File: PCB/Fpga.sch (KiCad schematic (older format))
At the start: 0 parts

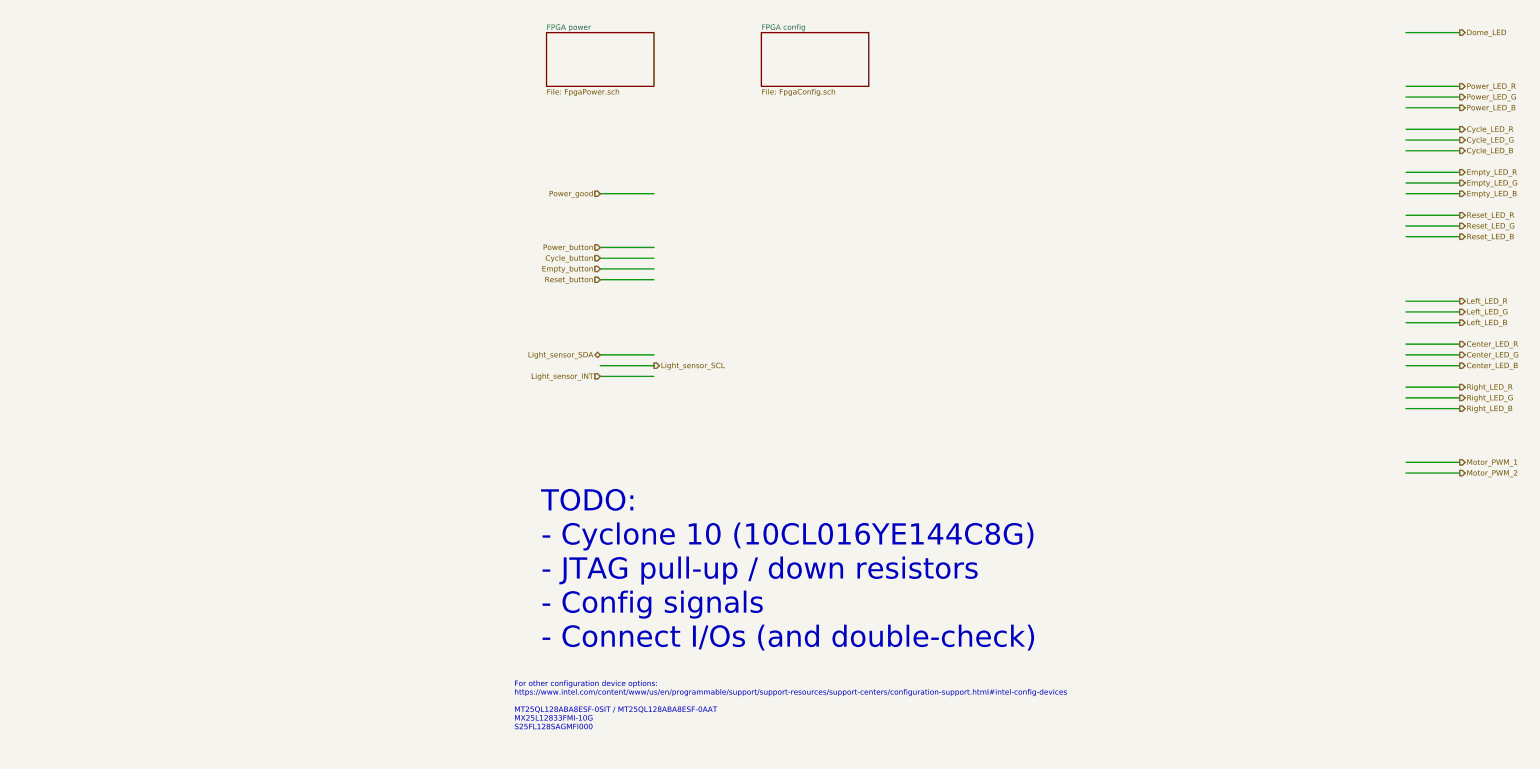
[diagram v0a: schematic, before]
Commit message: Connect the FPGA configuration signals
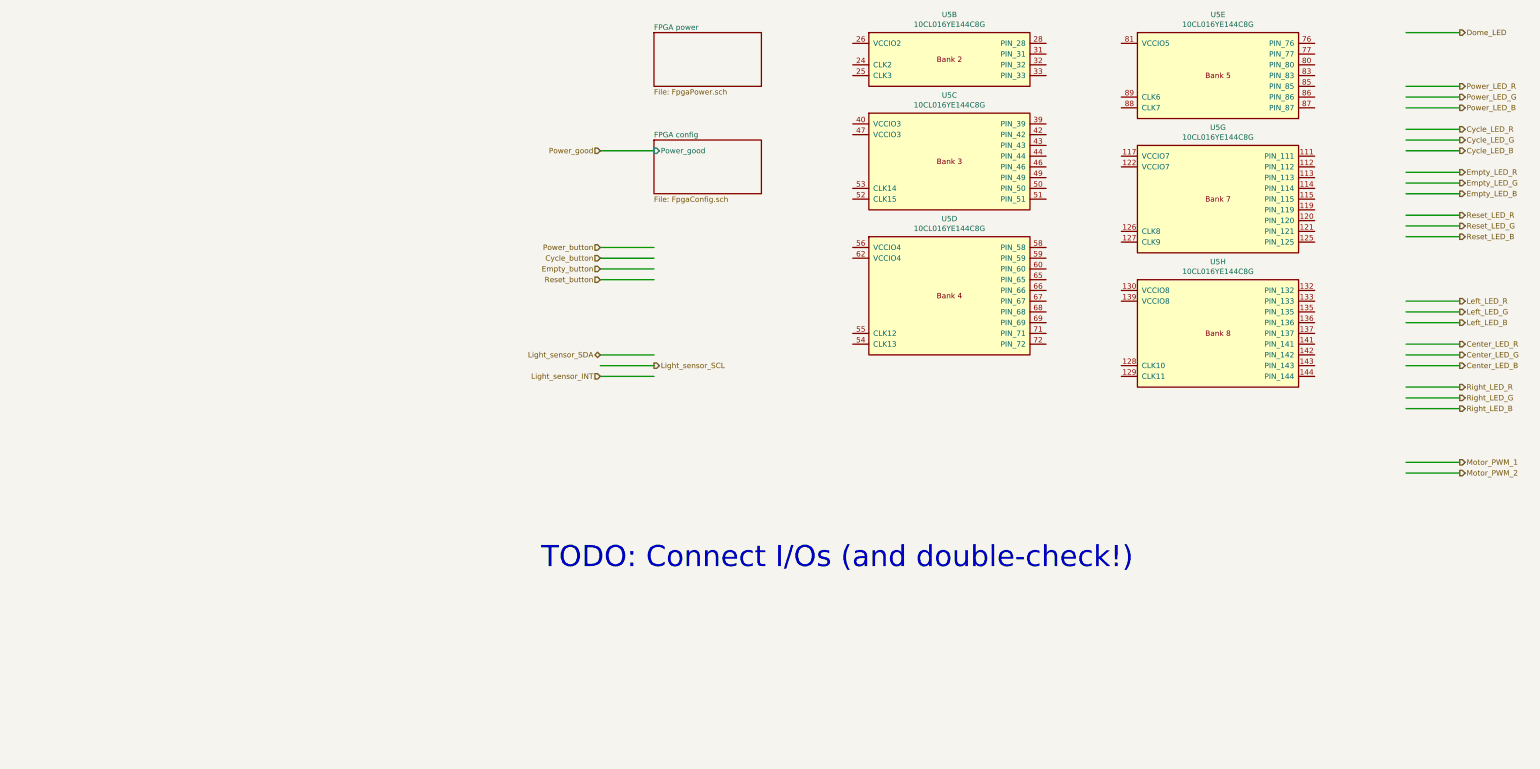
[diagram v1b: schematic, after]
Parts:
- added U5: 10CL016YE144C8G, LitterRobot:Intel_EQFP-144-1EP_20x20mm_P0.5mm_EP6.7x6.7mm, symbol LitterRobot:10CLxxxYE144
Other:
- note added: "TODO: Connect I/Os (and double-check!)"
- note removed: "For other configuration device options:\nhttps://www.intel.com/content/www/us/en/programmable/support/support-resources/support-centers/configuration-support.html#intel-config-devices\n\nMT25QL128ABA8ESF-0SIT / MT25QL128ABA8ESF-0AAT\nMX25L12833FMI-10G\nS25FL128SAGMFI000"
- note removed: "TODO:\n- Cyclone 10 (10CL016YE144C8G)\n- JTAG pull-up / down resistors\n- Config signals\n- Connect I/Os (and double-check)"
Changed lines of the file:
@@
 Wire Wire Line
 	1500 3300 2000 3300
-Text HLabel 1500 2500 0    50   Input ~ 0
+Text HLabel 1500 2100 0    50   Input ~ 0
 Power_good
 Wire Wire Line
-	1500 2500 2000 2500
+	1500 2100 2000 2100
 Wire Wire Line
 	9500 1700 9000 1700
@@
 Text HLabel 9500 5000 2    50   Output ~ 0
 Motor_PWM_1
-Text Notes 950  6750 0    197  ~ 0
-TODO:\n- Cyclone 10 (10CL016YE144C8G)\n- JTAG pull-up / down resistors\n- Config signals\n- Connect I/Os (and double-check)
+Text Notes 950  6000 0    197  ~ 0
+TODO: Connect I/Os (and double-check!)
 Wire Wire Line
 	9000 1000 9500 1000
@@
 Wire Wire Line
 	1500 4100 2000 4100
-Text Notes 700  7500 0    50   ~ 0
-For other configuration device options:\nhttps://www.intel.com/content/www/us/en/programmable/support/support-resources/support-centers/configuration-support.html#intel-config-devices\n\nMT25QL128ABA8ESF-0SIT / MT25QL128ABA8ESF-0AAT\nMX25L12833FMI-10G\nS25FL128SAGMFI000
 $Sheet
-S 3000 1000 1000 500
+S 2000 2000 1000 500
 U 60647CC2
 F0 "FPGA config" 50
 F1 "FpgaConfig.sch" 50
+F2 "Power_good" I L 2000 2100 50
 $EndSheet
 $Sheet
-S 1000 1000 1000 500
+S 2000 1000 1000 500
 U 60659E39
 F0 "FPGA power" 50
 F1 "FpgaPower.sch" 50
 $EndSheet
+$Comp
+L LitterRobot:10CLxxxYE144 U5
+U 2 1 60619400
+P 4750 1250
+F 0 "U5" H 4750 1667 50  0000 C CNN
+F 1 "10CL016YE144C8G" H 4750 1576 50  0000 C CNN
+F 2 "LitterRobot:Intel_EQFP-144-1EP_20x20mm_P0.5mm_EP6.7x6.7mm" H 4750 2000 50  0001 C CNN
+F 3 "https://www.intel.com/content/dam/www/programmable/us/en/pdfs/literature/hb/cyclone-10/c10lp-51003.pdf" H 4750 1350 50  0001 C CNN
+F 4 "10CL016YE144C8G" H 4750 1250 50  0001 C CNN "Part_number"
+	2    4750 1250
+	1    0    0    -1
+$EndComp
+$Comp
+L LitterRobot:10CLxxxYE144 U5
+U 3 1 6061BBFB
+P 4750 2200
+F 0 "U5" H 4750 2817 50  0000 C CNN
+F 1 "10CL016YE144C8G" H 4750 2726 50  0000 C CNN
+F 2 "LitterRobot:Intel_EQFP-144-1EP_20x20mm_P0.5mm_EP6.7x6.7mm" H 4750 2950 50  0001 C CNN
+F 3 "https://www.intel.com/content/dam/www/programmable/us/en/pdfs/literature/hb/cyclone-10/c10lp-51003.pdf" H 4750 2300 50  0001 C CNN
+F 4 "10CL016YE144C8G" H 4750 2200 50  0001 C CNN "Part_number"
+	3    4750 2200
+	1    0    0    -1
+$EndComp
+$Comp
+L LitterRobot:10CLxxxYE144 U5
+U 4 1 6061E40A
+P 4750 3450
+F 0 "U5" H 4750 4167 50  0000 C CNN
+F 1 "10CL016YE144C8G" H 4750 4076 50  0000 C CNN
+F 2 "LitterRobot:Intel_EQFP-144-1EP_20x20mm_P0.5mm_EP6.7x6.7mm" H 4750 4200 50  0001 C CNN
+F 3 "https://www.intel.com/content/dam/www/programmable/us/en/pdfs/literature/hb/cyclone-10/c10lp-51003.pdf" H 4750 3550 50  0001 C CNN
+F 4 "10CL016YE144C8G" H 4750 3450 50  0001 C CNN "Part_number"
+	4    4750 3450
+	1    0    0    -1
+$EndComp
+$Comp
+L LitterRobot:10CLxxxYE144 U5
+U 5 1 60620AE3
+P 7250 1400
+F 0 "U5" H 7250 1967 50  0000 C CNN
+F 1 "10CL016YE144C8G" H 7250 1876 50  0000 C CNN
+F 2 "LitterRobot:Intel_EQFP-144-1EP_20x20mm_P0.5mm_EP6.7x6.7mm" H 7250 2150 50  0001 C CNN
+F 3 "https://www.intel.com/content/dam/www/programmable/us/en/pdfs/literature/hb/cyclone-10/c10lp-51003.pdf" H 7250 1500 50  0001 C CNN
+F 4 "10CL016YE144C8G" H 7250 1400 50  0001 C CNN "Part_number"
+	5    7250 1400
+	1    0    0    -1
+$EndComp
+$Comp
+L LitterRobot:10CLxxxYE144 U5
+U 7 1 60623EE0
+P 7250 2550
+F 0 "U5" H 7250 3217 50  0000 C CNN
+F 1 "10CL016YE144C8G" H 7250 3126 50  0000 C CNN
+F 2 "LitterRobot:Intel_EQFP-144-1EP_20x20mm_P0.5mm_EP6.7x6.7mm" H 7250 3300 50  0001 C CNN
+F 3 "https://www.intel.com/content/dam/www/programmable/us/en/pdfs/literature/hb/cyclone-10/c10lp-51003.pdf" H 7250 2650 50  0001 C CNN
+F 4 "10CL016YE144C8G" H 7250 2550 50  0001 C CNN "Part_number"
+	7    7250 2550
+	1    0    0    -1
+$EndComp
+$Comp
+L LitterRobot:10CLxxxYE144 U5
+U 8 1 6062761C
+P 7250 3800
+F 0 "U5" H 7250 4467 50  0000 C CNN
+F 1 "10CL016YE144C8G" H 7250 4376 50  0000 C CNN
+F 2 "LitterRobot:Intel_EQFP-144-1EP_20x20mm_P0.5mm_EP6.7x6.7mm" H 7250 4550 50  0001 C CNN
+F 3 "https://www.intel.com/content/dam/www/programmable/us/en/pdfs/literature/hb/cyclone-10/c10lp-51003.pdf" H 7250 3900 50  0001 C CNN
+F 4 "10CL016YE144C8G" H 7250 3800 50  0001 C CNN "Part_number"
+	8    7250 3800
+	1    0    0    -1
+$EndComp
 $EndSCHEMATC

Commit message: Cleaned up the schematics
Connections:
- net labels added: +3V3, Extension1, Extension2, Extension3, Extension4, GND
- wire segments 32 -> 80
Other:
- note removed: "TODO: Connect I/Os (and double-check!)"
- moved on the sheet: U5E, U5G, U5H

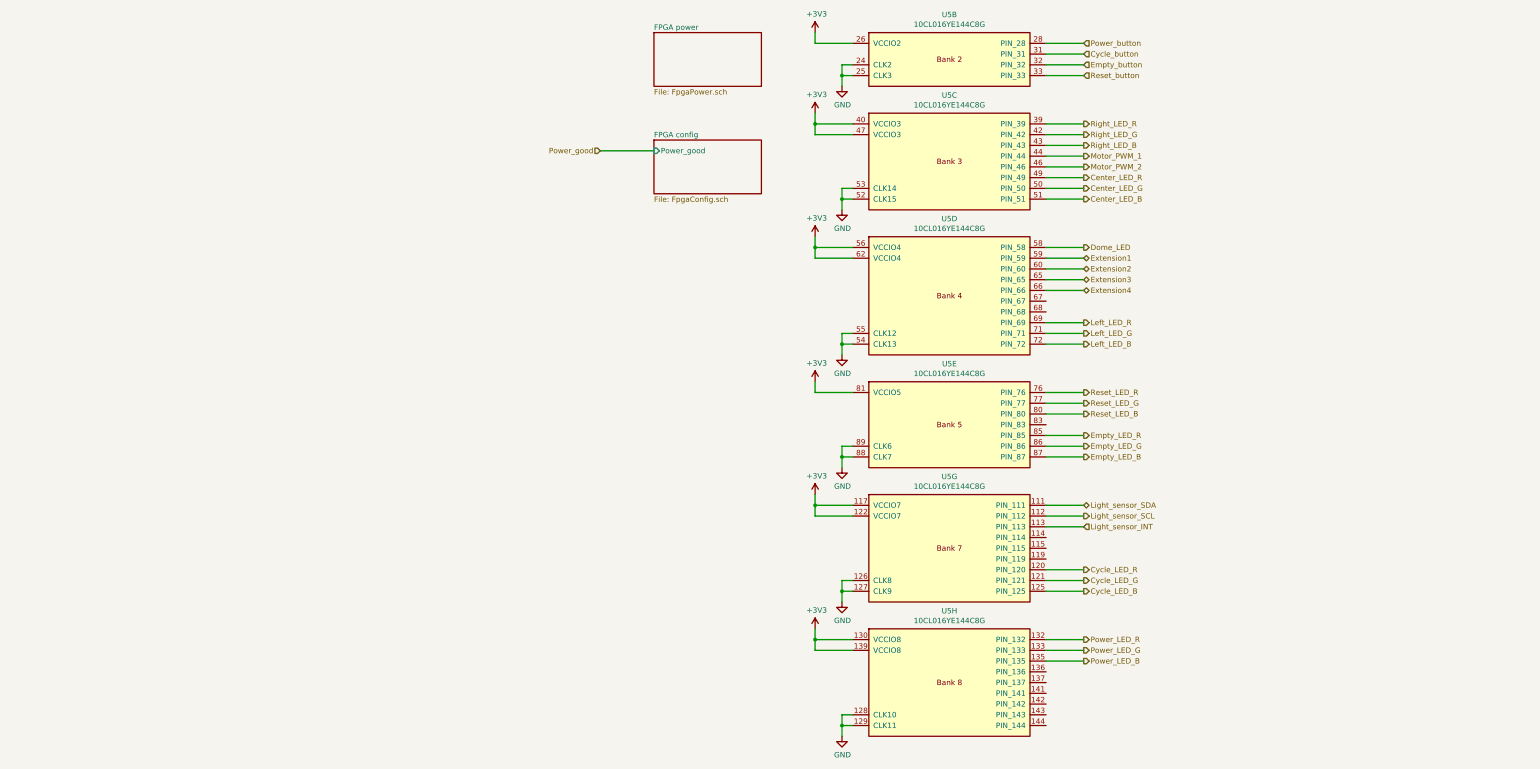
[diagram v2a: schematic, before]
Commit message: Plot the schematic as PDF
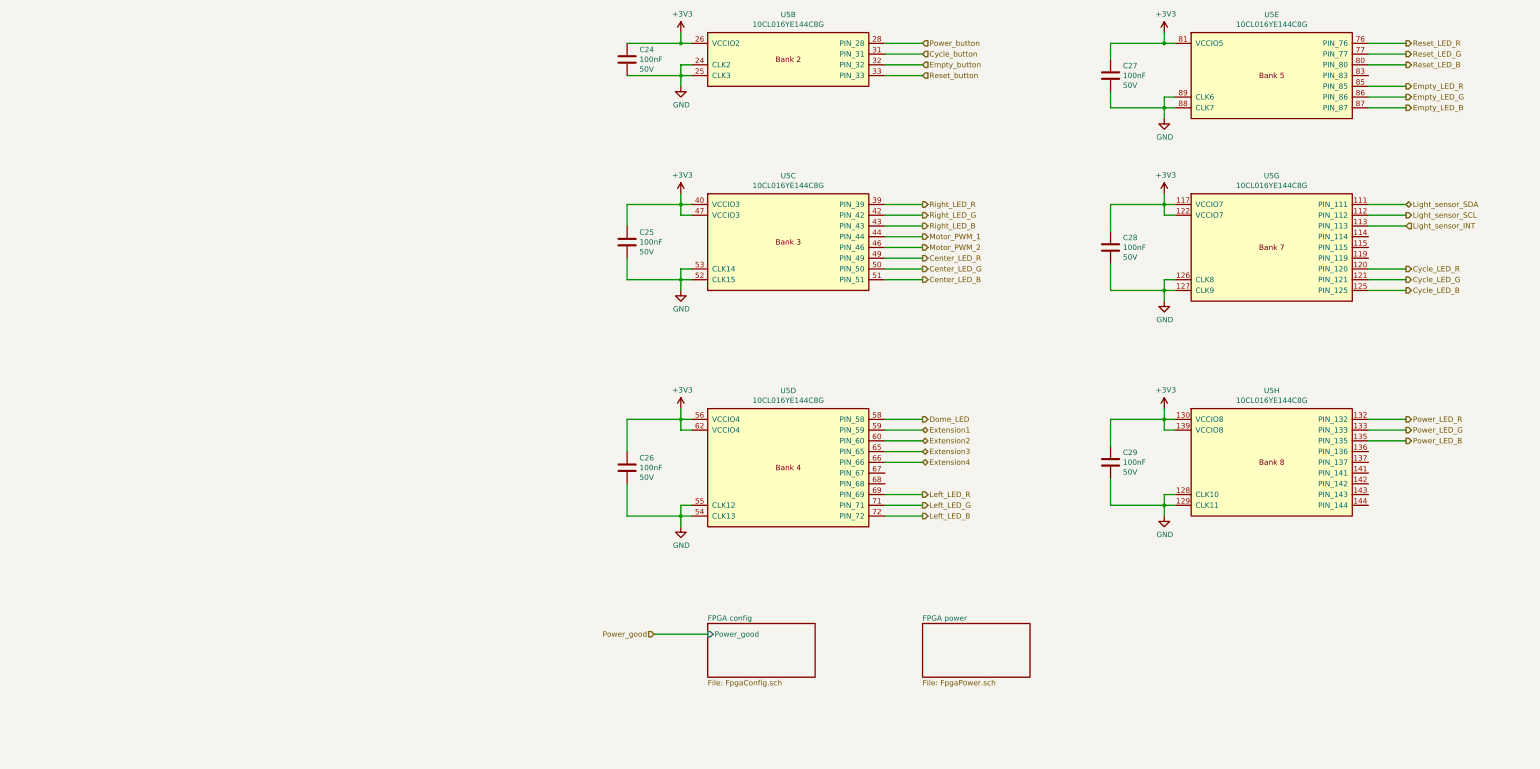
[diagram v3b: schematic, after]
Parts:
- added C24, C25, C26, C27, C28, C29: 100nF, Capacitor_SMD:C_0603_1608Metric, symbol Device:C
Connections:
- net +3V3: now also C24.1, C25.1, C26.1, C27.1, C28.1, C29.1
- net GND: now also C24.2, C25.2, C26.2, C27.2, C28.2, C29.2
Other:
- moved on the sheet: U5B, U5C, U5D, U5E, U5G, U5H

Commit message: Add support for the weight sensor
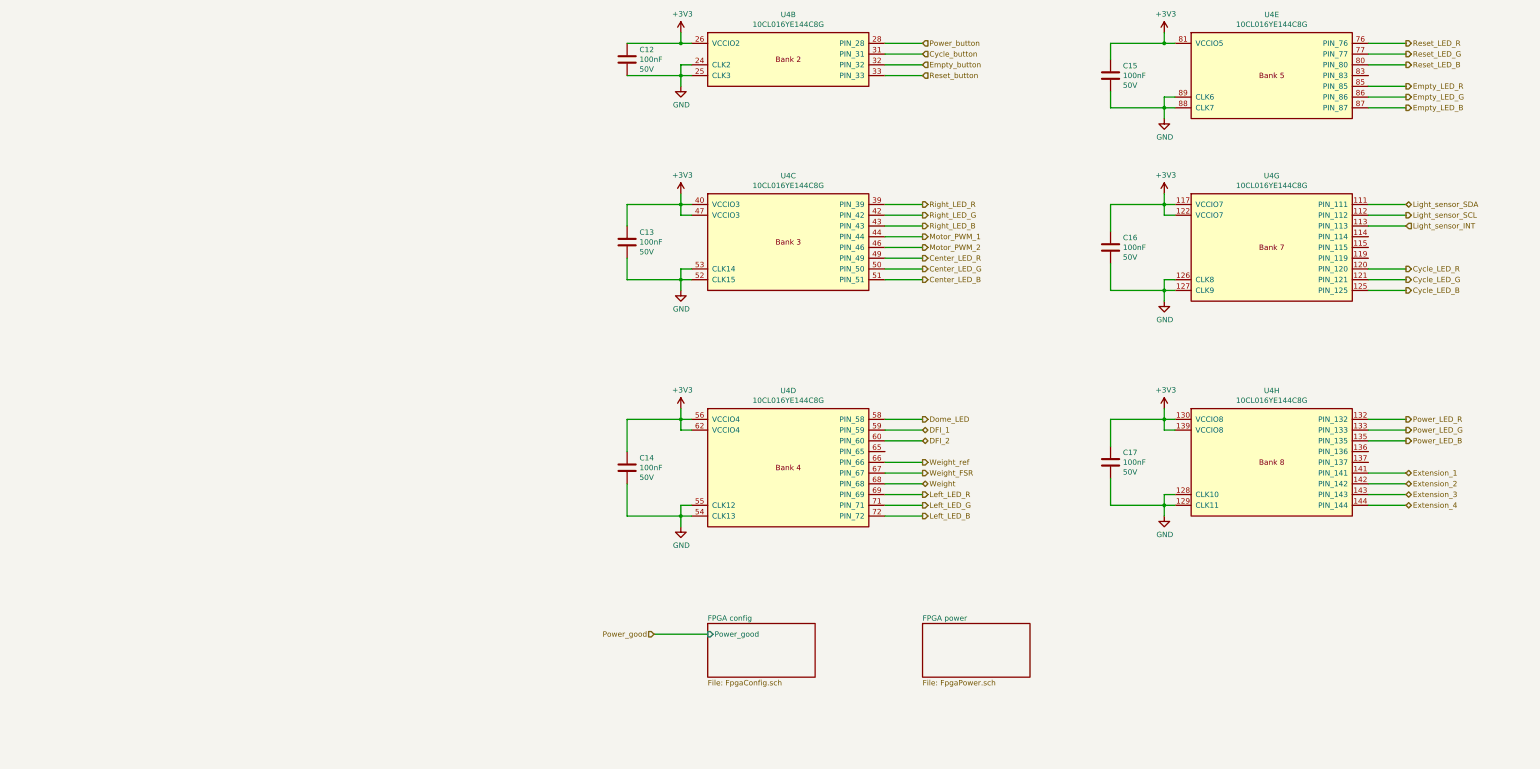
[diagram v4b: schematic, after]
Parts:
- renumbered C24 to C12, C25 to C13, C26 to C14, C27 to C15, C28 to C16, C29 to C17, U5 to U4
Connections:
- net Weight_FSR: now reaches U4.67 (PIN_67)
- net Weight: now reaches U4.68 (PIN_68)
- net Extension_1: now reaches U4.141 (PIN_141)
- net Extension_2: now reaches U4.142 (PIN_142)
- net Extension_3: now reaches U4.143 (PIN_143)
- net Extension_4: now reaches U4.144 (PIN_144)
- net Extension1 renamed DFI_1
- net Extension2 renamed DFI_2
- net Extension3: no longer names the net of U4.65 (PIN_65)
- net Extension4 renamed Weight_ref
